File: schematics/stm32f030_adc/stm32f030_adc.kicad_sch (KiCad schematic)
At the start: 26 parts, among them J1 SWD, J2 AudioJack3, U1 STM32F103C6Tx, U2 AMS1117-3.3, U3 OPAMP, U4 OPAMP, X1 USB_B_Micro

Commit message: [stm32f030_adc:stm32f030_adc] Impl |
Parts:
- added C10: 1 uF, symbol Device:C
- added R11: 10k, symbol pspice:R
- U3, U4: value OPAMP -> ${SIM.PARAMS}; Spice_Netlist_Enabled Y -> (none); Spice_Primitive X -> (none)
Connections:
- net +3V3: now also R11.1
- net GNDREF: now also U1.44 (BOOT0), C10.2
- net at U1.7 (NRST): now also C10.1, R11.2

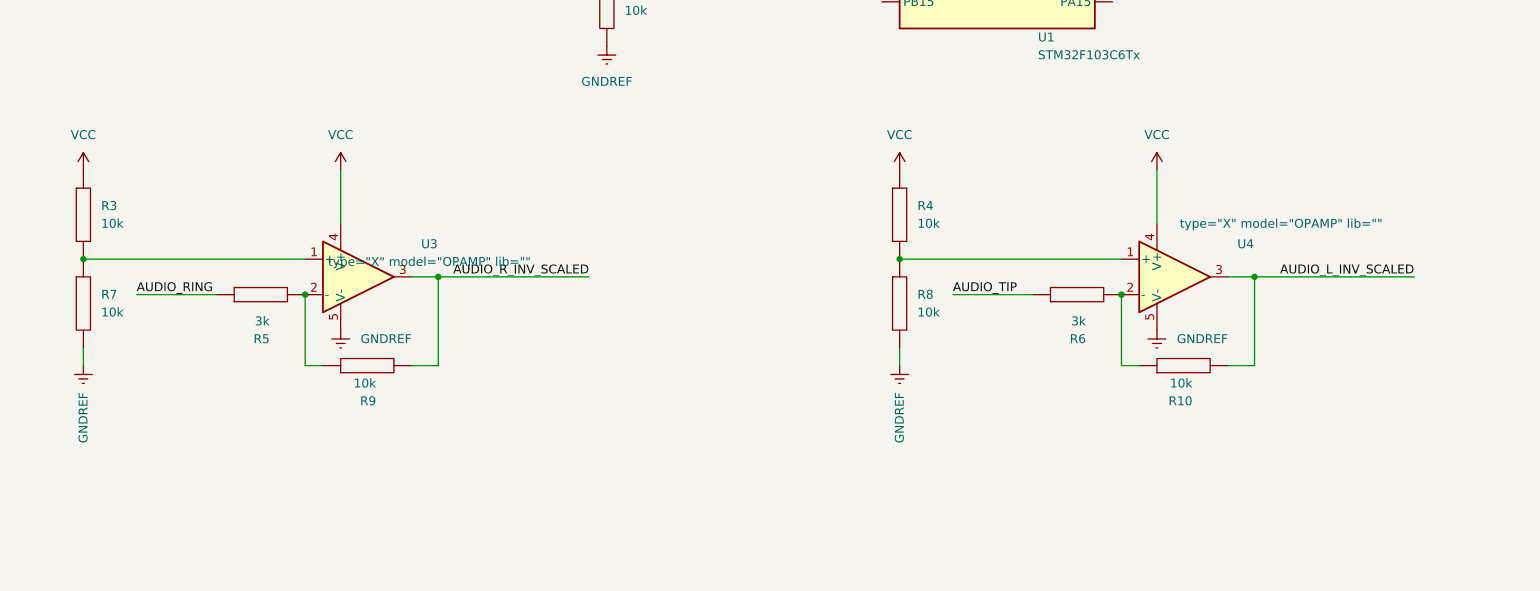
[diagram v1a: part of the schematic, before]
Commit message: [schematics:stm32f030_adc] Impl | Replaced generic OpAmp w/ TL072CP
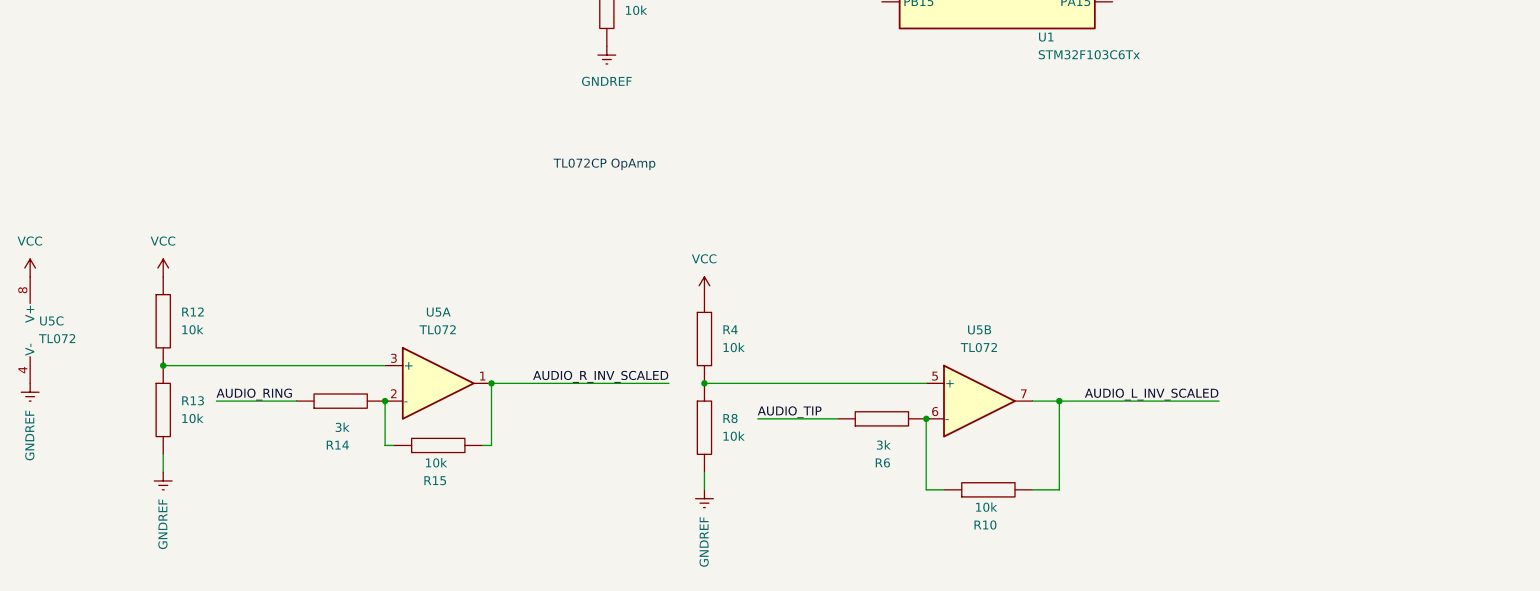
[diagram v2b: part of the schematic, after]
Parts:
- removed R3, R7, R9: 10k, symbol pspice:R
- removed R5: 3k, symbol pspice:R
- removed U3, U4: ${SIM.PARAMS}, symbol Simulation_SPICE:OPAMP
- added R12, R13, R15: 10k, symbol pspice:R
- added R14: 3k, symbol pspice:R
- added U5: TL072, symbol Amplifier_Operational:TL072
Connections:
- net AUDIO_L_INV_SCALED: now also U5.7
- net AUDIO_RING: now also R14.1
- net AUDIO_R_INV_SCALED: now also R15.2, U5.1
- net GNDREF: now also R13.2, U5.4 (V-)
- net VCC: now also R12.1, U5.8 (V+)
- net at R10.1, R6.2: now also U5.6 (-)
- net at R4.2, R8.1: now also U5.5 (+)
- new net: R14.2, R15.1, U5.2 (-)
- new net: R12.2, R13.1, U5.3 (+)
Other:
- note added: "TL072CP OpAmp"
- moved on the sheet: R10, R4, R6, R8

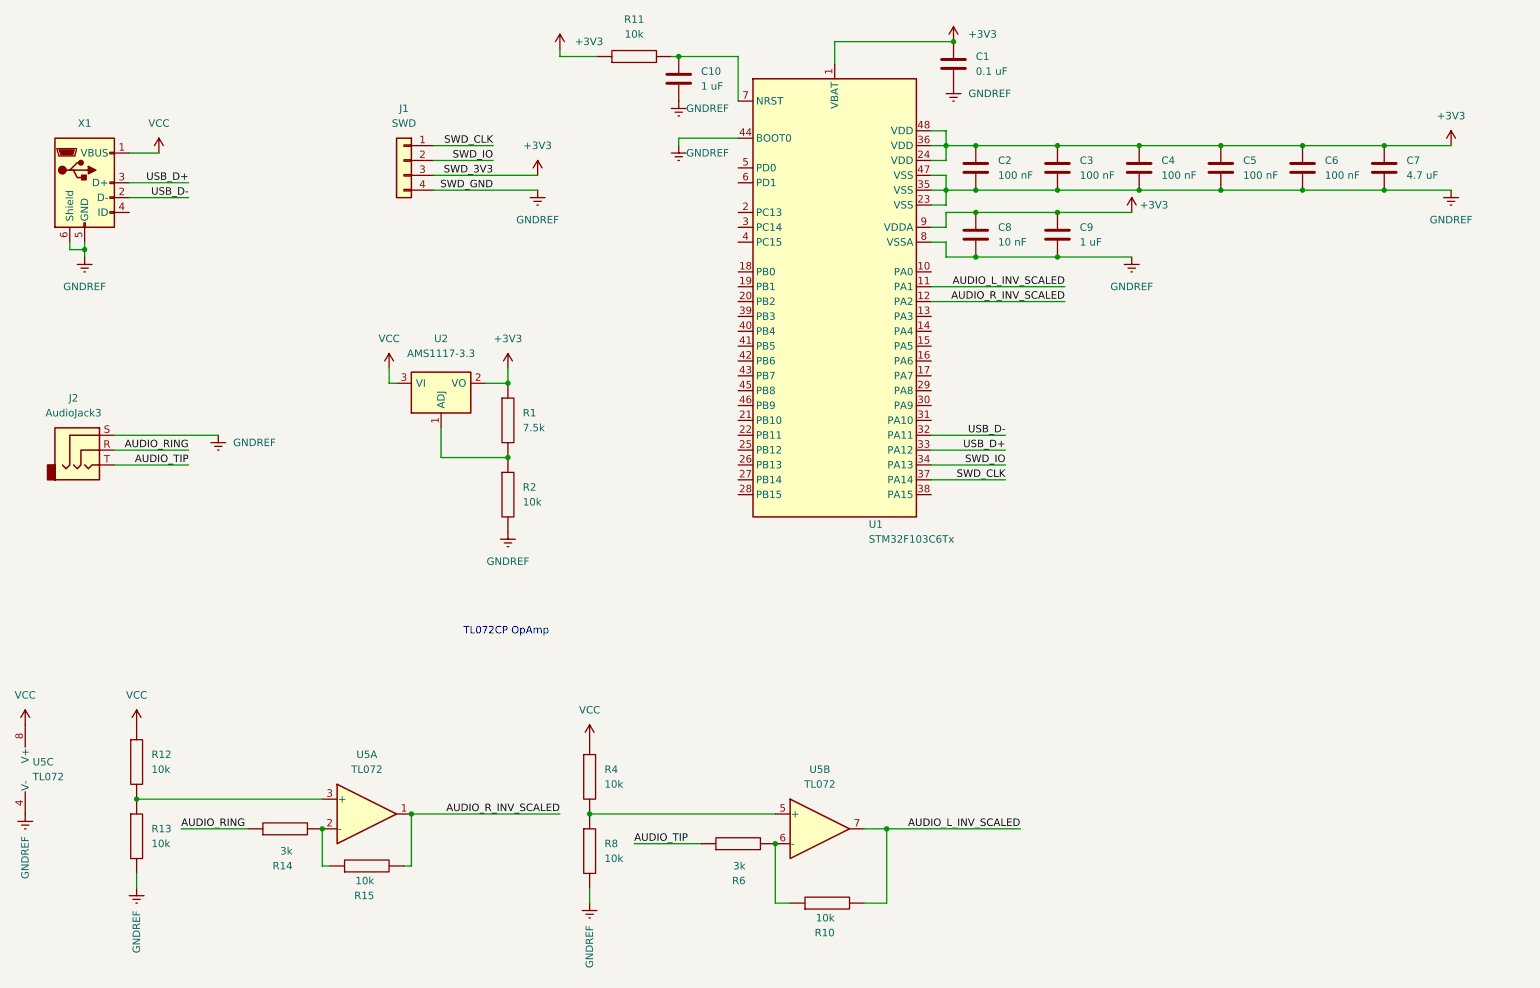
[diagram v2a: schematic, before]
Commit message: [stm32f030_adc:*] Impl | Organized sheets in hierarchical manner
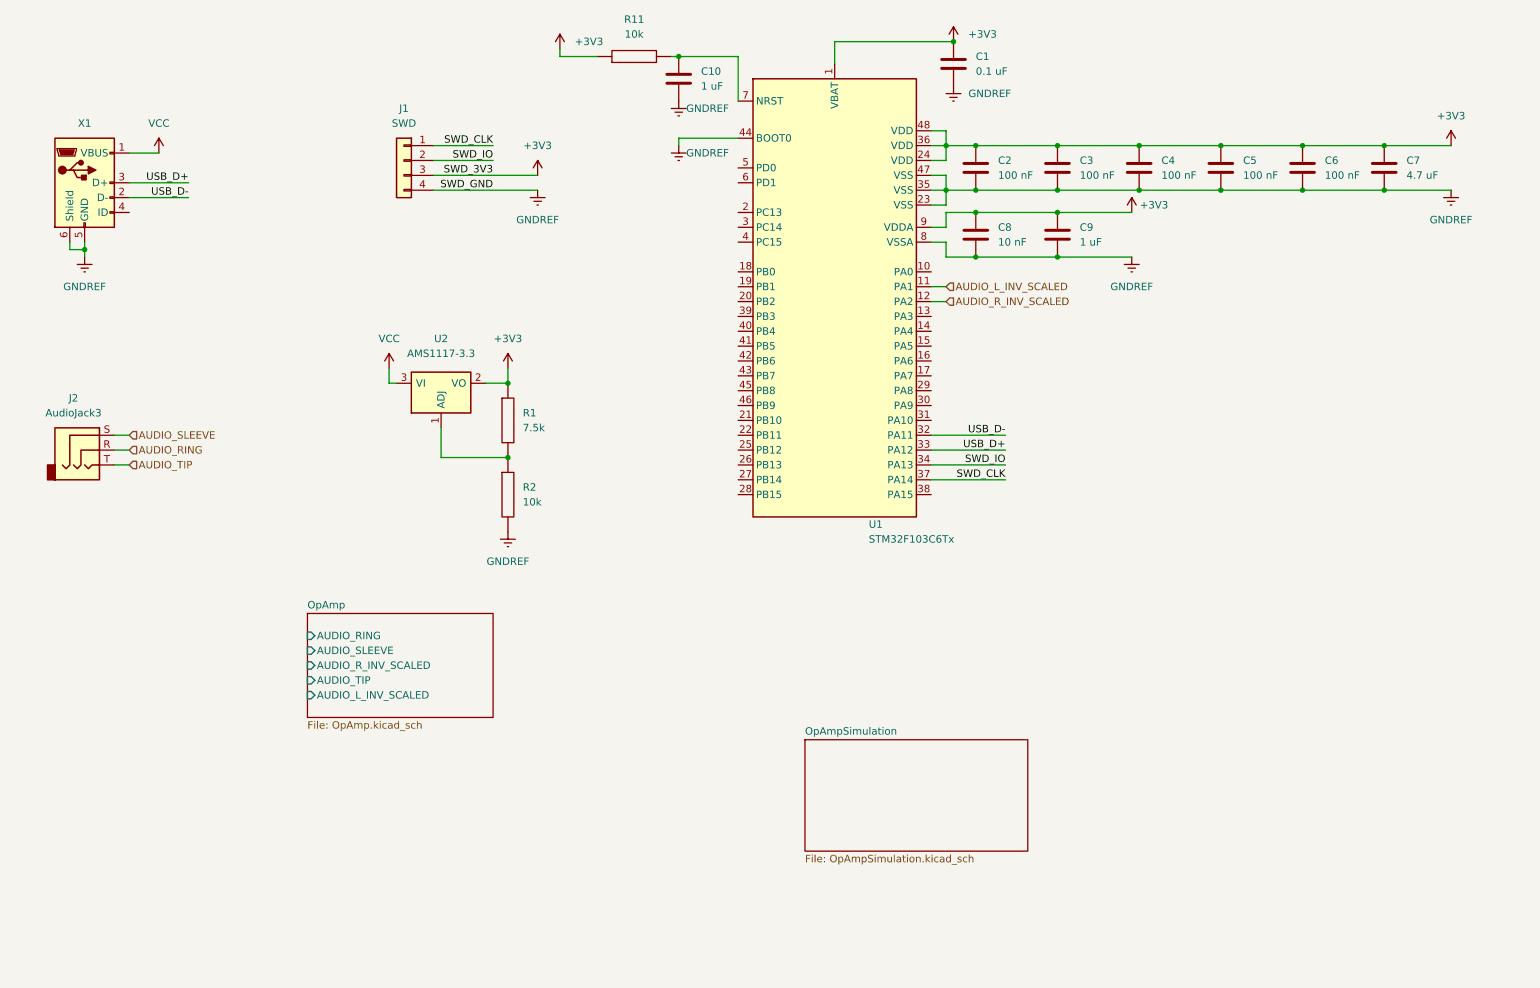
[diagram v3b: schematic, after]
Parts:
- removed R10, R12, R13, R15, R4, R8: 10k, symbol pspice:R
- removed R14, R6: 3k, symbol pspice:R
- removed U5: TL072, symbol Amplifier_Operational:TL072
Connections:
- net GNDREF: no longer J2.S
- new net AUDIO_SLEEVE: J2.S
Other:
- added sheet OpAmp (OpAmp.kicad_sch)
- added sheet OpAmpSimulation (OpAmpSimulation.kicad_sch)
- note removed: "TL072CP OpAmp"

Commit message: [schematics:*] Bug | Fixed OpAmp schematics based on the simulation and practical experiments' results
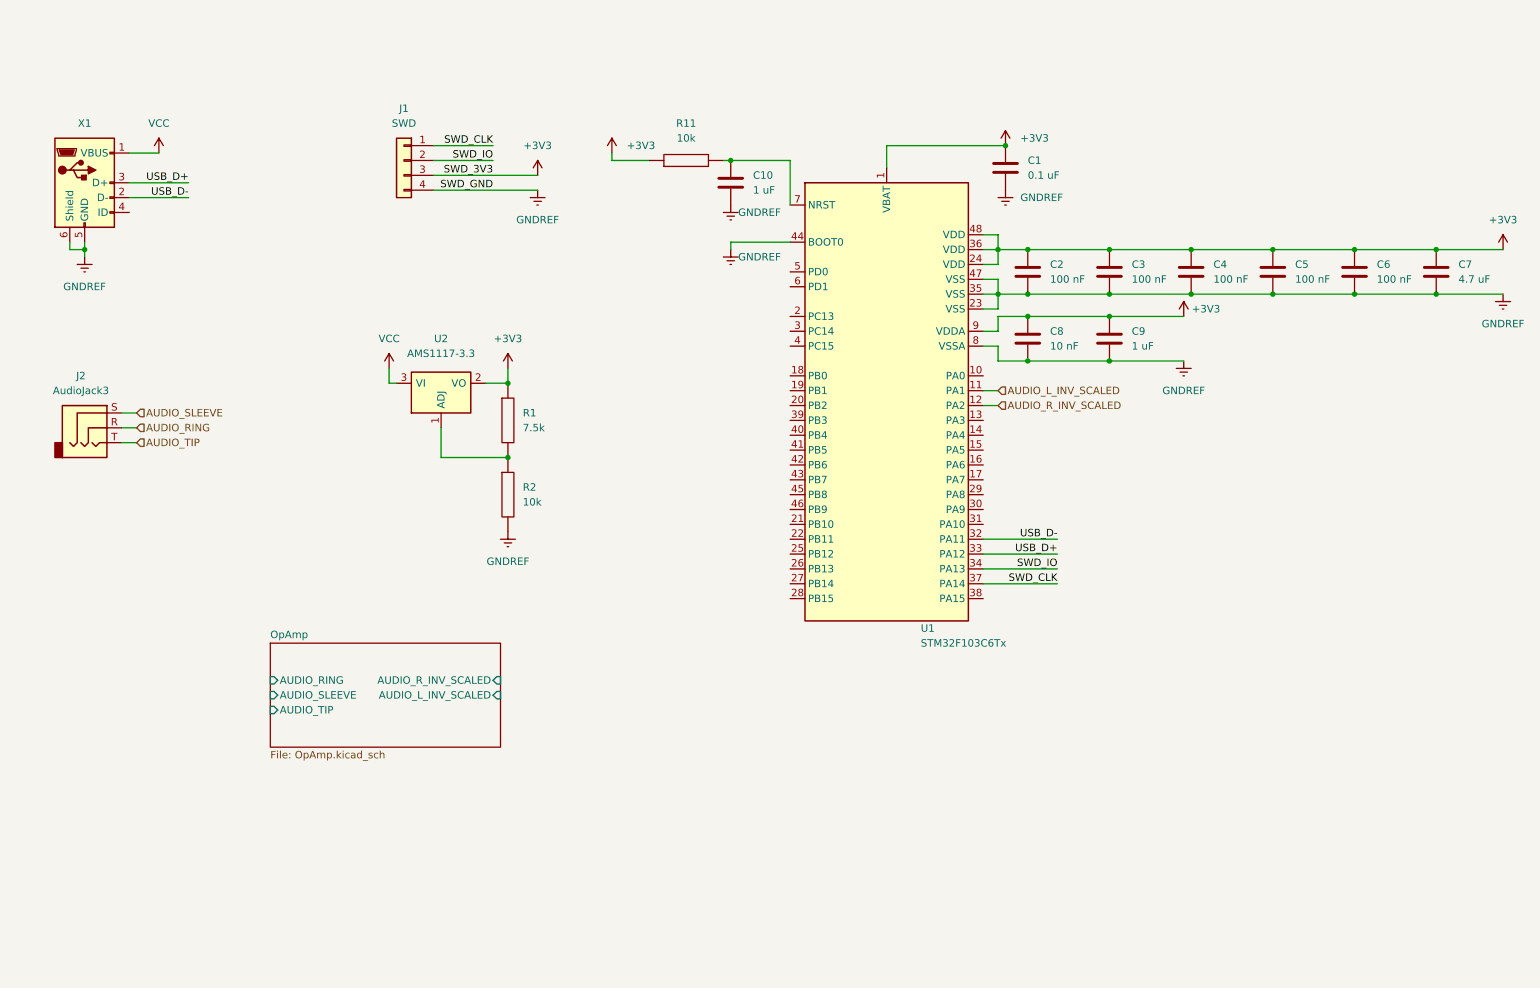
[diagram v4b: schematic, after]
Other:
- removed sheet OpAmpSimulation
- moved on the sheet: C1, C10, C2, C3, C4, C5, C6, C7, C8, C9, J2, R11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

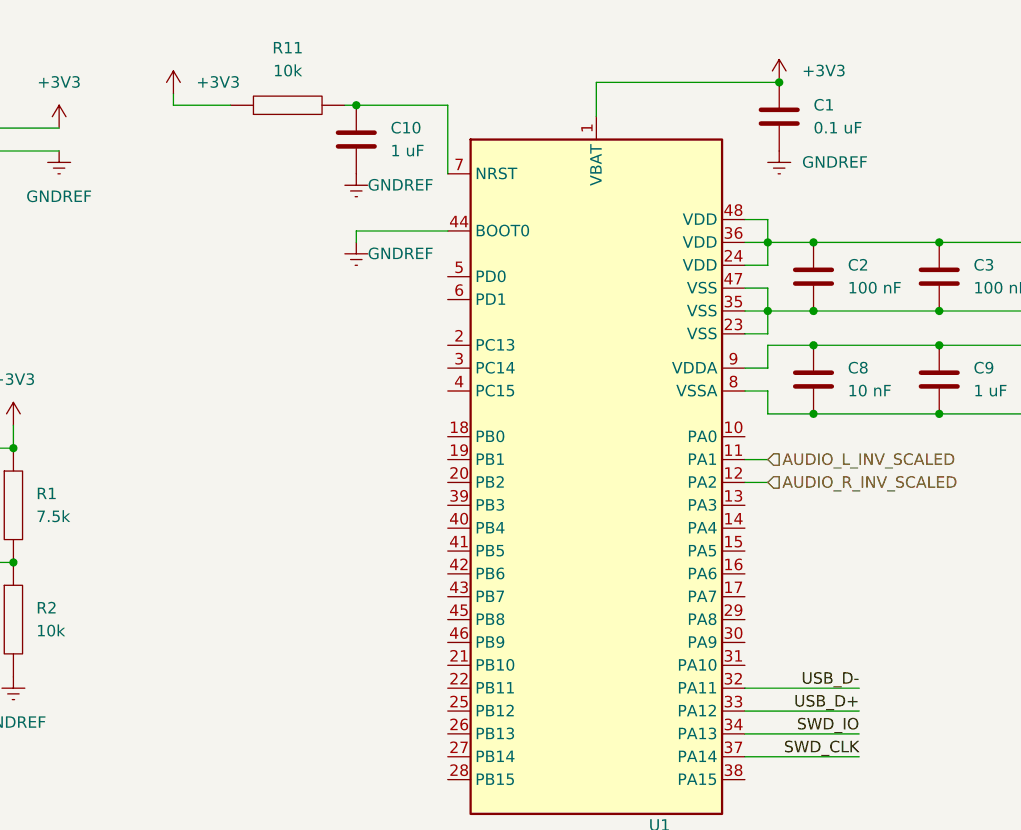
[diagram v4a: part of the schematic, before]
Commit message: [schematics:stm32f030_adc] Impl | Added UART on PA9, PA10
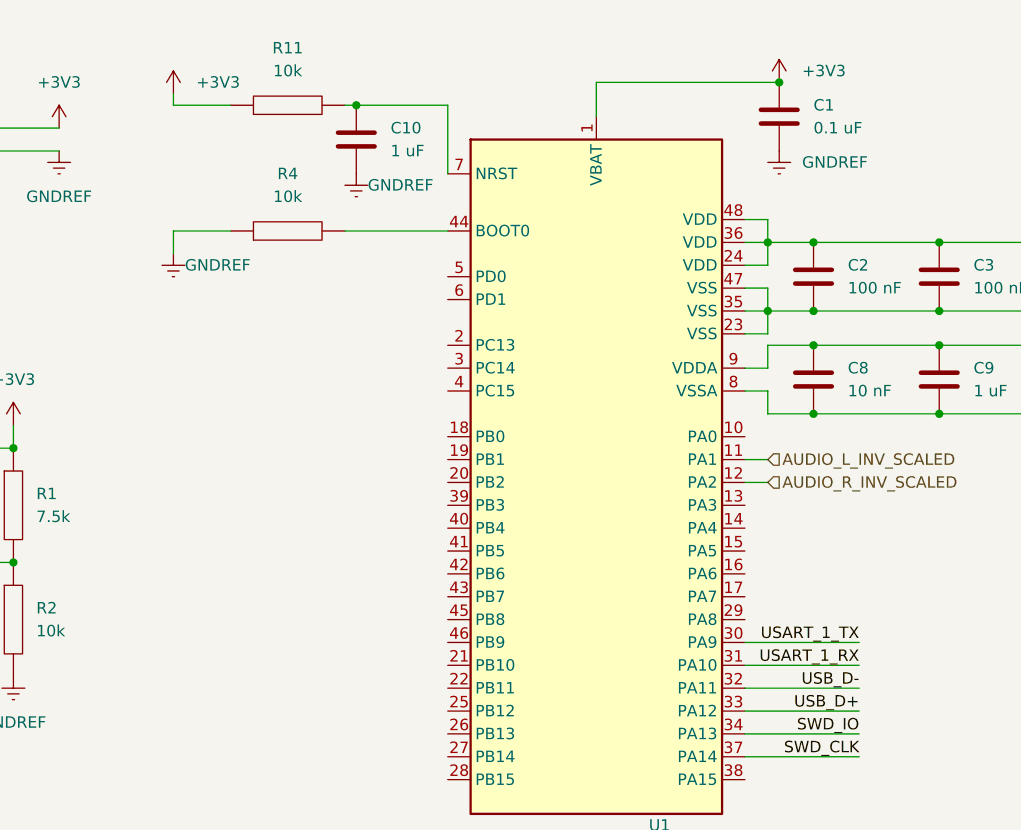
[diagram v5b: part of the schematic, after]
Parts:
- added R4: 10k, symbol pspice:R
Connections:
- net GNDREF: now also R4.1; no longer U1.44 (BOOT0)
- net USART_1_TX: now reaches U1.30 (PA9)
- net USART_1_RX: now reaches U1.31 (PA10)
- new net: R4.2, U1.44 (BOOT0)
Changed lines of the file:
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@@
     (stroke (width 0) (type default))
   )
-  (wire (pts (xy 144.78 53.34) (xy 144.78 54.61))
+  (wire (pts (xy 124.46 53.34) (xy 124.46 55.88))
     (stroke (width 0) (type default))
   )
@@
     (stroke (width 0) (type default))
   )
+  (wire (pts (xy 130.81 53.34) (xy 124.46 53.34))
+    (stroke (width 0) (type default))
+  )
   (wire (pts (xy 102.87 77.47) (xy 106.68 77.47))
     (stroke (width 0) (type default))
@@
     (stroke (width 0) (type default))
   )
-  (wire (pts (xy 154.94 53.34) (xy 144.78 53.34))
+  (wire (pts (xy 154.94 53.34) (xy 143.51 53.34))
+    (stroke (width 0) (type default))
+  )
+  (wire (pts (xy 187.96 99.06) (xy 200.66 99.06))
     (stroke (width 0) (type default))
   )
@@
     (stroke (width 0) (type default))
   )
+  (wire (pts (xy 187.96 101.6) (xy 200.66 101.6))
+    (stroke (width 0) (type default))
+  )
   (wire (pts (xy 187.96 62.23) (xy 190.5 62.23))
     (stroke (width 0) (type default))
@@
     (effects (font (size 1.27 1.27)) (justify right bottom))
   )
+  (label "USART_1_TX" (at 200.66 99.06 180) (fields_autoplaced)
+    (effects (font (size 1.27 1.27)) (justify right bottom))
+  )
   (label "SWD_3V3" (at 104.14 41.91 180) (fields_autoplaced)
     (effects (font (size 1.27 1.27)) (justify right bottom))
   )
   (label "SWD_IO" (at 200.66 109.22 180) (fields_autoplaced)
+    (effects (font (size 1.27 1.27)) (justify right bottom))
+  )
+  (label "USART_1_RX" (at 200.66 101.6 180) (fields_autoplaced)
     (effects (font (size 1.27 1.27)) (justify right bottom))
   )
@@
     )
   )
+  (symbol (lib_id "pspice:R") (at 137.16 53.34 90) (unit 1)
+    (in_bom yes) (on_board yes) (dnp no) (fields_autoplaced)
+    (property "Reference" "R4" (at 137.16 46.99 90)
+      (effects (font (size 1.27 1.27)))
+    )
+    (property "Value" "10k" (at 137.16 49.53 90)
+      (effects (font (size 1.27 1.27)))
+    )
+    (property "Footprint" "" (at 137.16 53.34 0)
+      (effects (font (size 1.27 1.27)) hide)
+    )
+    (property "Datasheet" "~" (at 137.16 53.34 0)
+      (effects (font (size 1.27 1.27)) hide)
+    )
+    (pin "1")
+    (pin "2")
+    (instances
+      (project "stm32f030_adc"
+        (path "/85629656-c73b-4e1f-b8e8-4366f4b01266"
+          (reference "R4") (unit 1)
+        )
+      )
+    )
+  )
   (symbol (lib_id "Device:C") (at 195.58 58.42 0) (unit 1)
     (in_bom yes) (on_board yes) (dnp no) (fields_autoplaced)
@@
     )
   )
-  (symbol (lib_id "power:GNDREF") (at 144.78 54.61 0) (unit 1)
+  (symbol (lib_id "power:GNDREF") (at 124.46 55.88 0) (unit 1)
     (in_bom yes) (on_board yes) (dnp no)
-    (property "Reference" "#PWR03" (at 144.78 60.96 0)
-      (effects (font (size 1.27 1.27)) hide)
-    )
-    (property "Value" "GNDREF" (at 146.05 55.88 0)
-      (effects (font (size 1.27 1.27)) (justify left))
-    )
-    (property "Footprint" "" (at 144.78 54.61 0)
-      (effects (font (size 1.27 1.27)) hide)
-    )
-    (property "Datasheet" "" (at 144.78 54.61 0)
-      (effects (font (size 1.27 1.27)) hide)
-    )
+    (property "Reference" "#PWR03" (at 124.46 62.23 0)
+      (effects (font (size 1.27 1.27)) hide)
+    )
+    (property "Value" "GNDREF" (at 125.73 57.15 0)
+      (effects (font (size 1.27 1.27)) (justify left))
+    )
+    (property "Footprint" "" (at 124.46 55.88 0)
+      (effects (font (size 1.27 1.27)) hide)
+    )
+    (property "Datasheet" "" (at 124.46 55.88 0)
+      (effects (font (size 1.27 1.27)) hide)
+    )
